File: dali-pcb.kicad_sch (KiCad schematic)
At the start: 2 parts

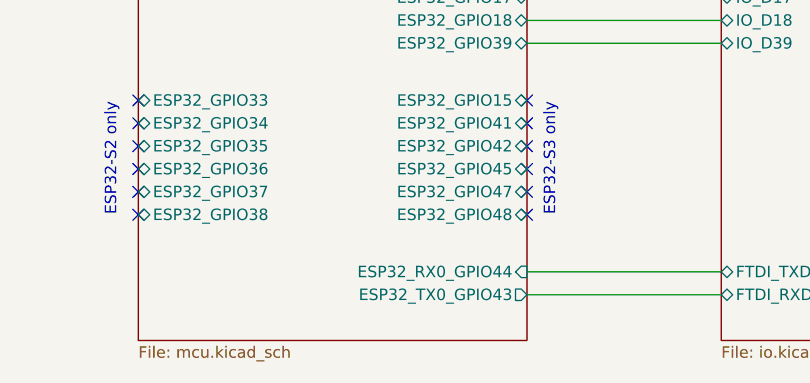
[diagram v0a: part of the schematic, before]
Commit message: Rename UART pins to use Espressif convention
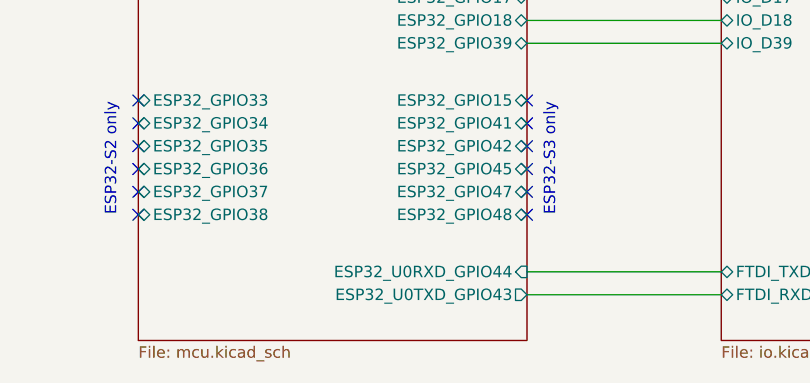
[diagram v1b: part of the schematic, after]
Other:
- sheet Microcontroller ports: added ESP32_U0RXD_GPIO44, ESP32_U0TXD_GPIO43; removed ESP32_RX0_GPIO44, ESP32_TX0_GPIO43
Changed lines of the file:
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@@
 			)
 		)
-		(pin "ESP32_RX0_GPIO44" input
+		(pin "ESP32_U0RXD_GPIO44" input
 			(at 144.78 82.55 0)
 			(effects
@@
 			)
 		)
-		(pin "ESP32_TX0_GPIO43" output
+		(pin "ESP32_U0TXD_GPIO43" output
 			(at 144.78 85.09 0)
 			(effects

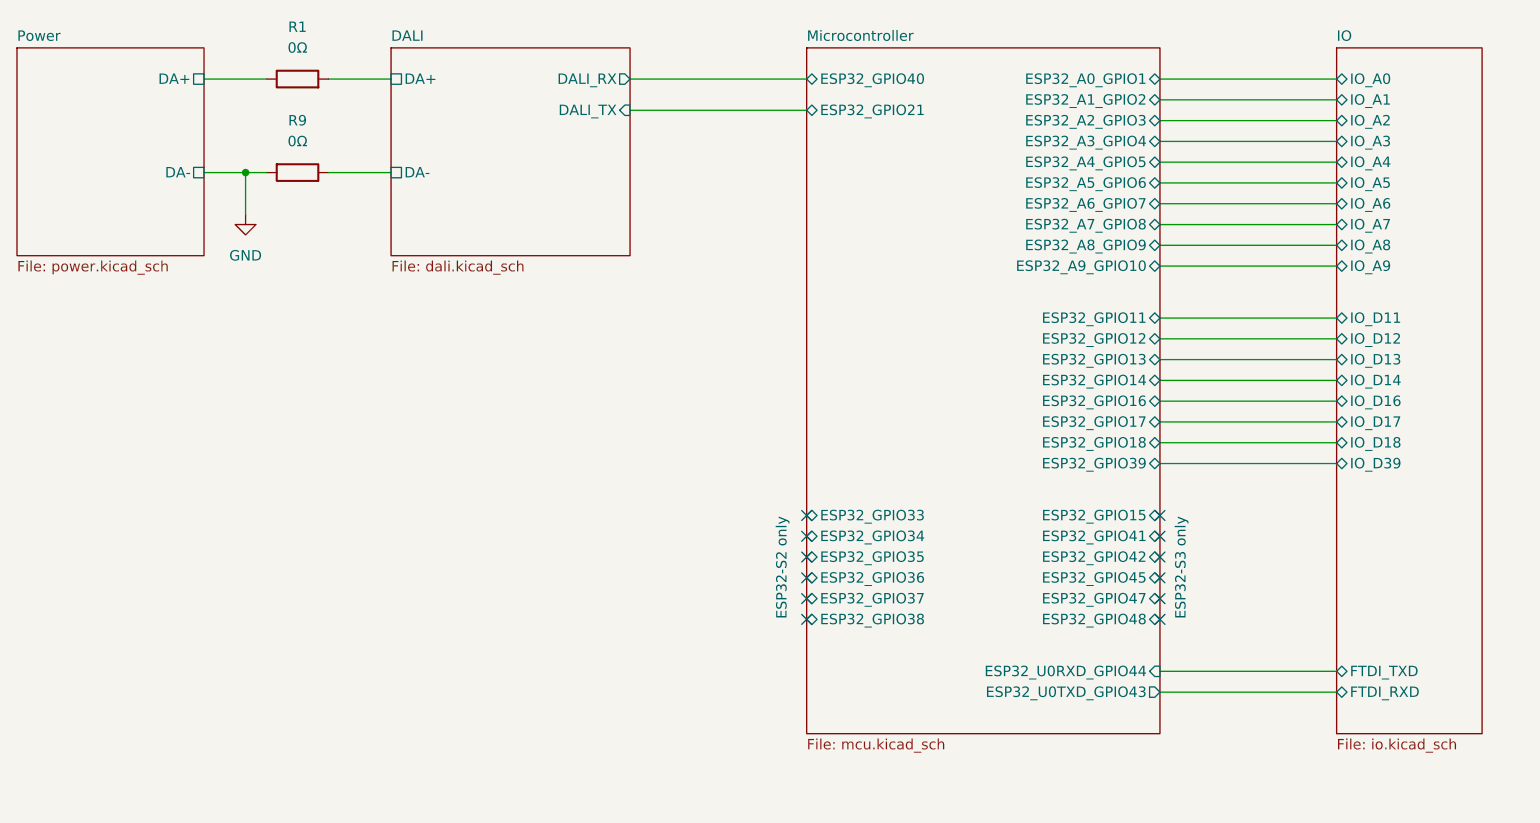
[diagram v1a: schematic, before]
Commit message: Add an FTDI connector for the DALI bus
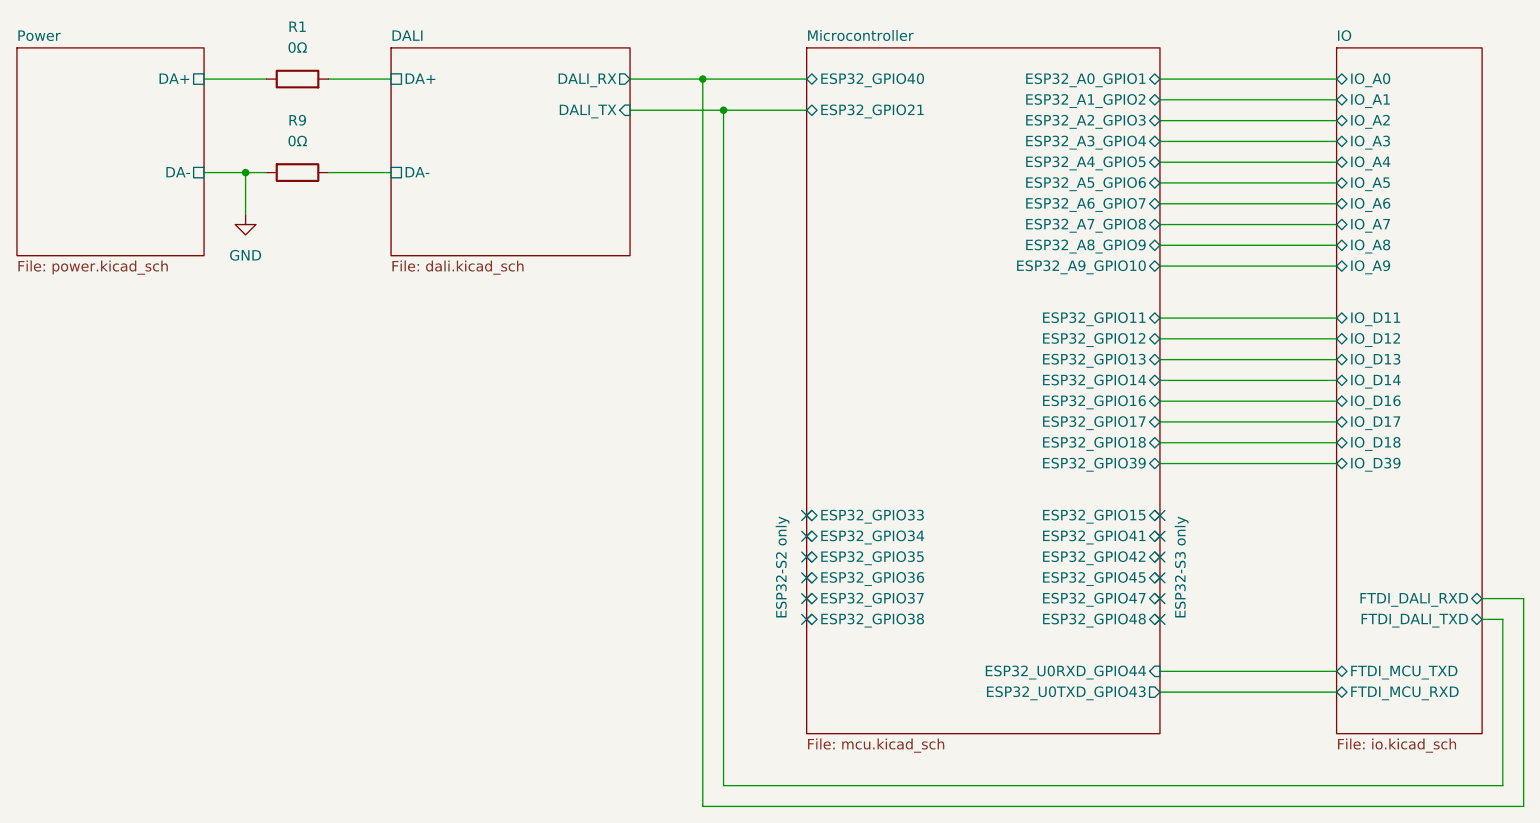
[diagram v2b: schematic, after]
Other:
- sheet IO ports: added FTDI_DALI_RXD, FTDI_DALI_TXD, FTDI_MCU_RXD, FTDI_MCU_TXD; removed FTDI_RXD, FTDI_TXD
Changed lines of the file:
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@@
 	(generator "eeschema")
 	(generator_version "9.0")
-	(paper "User" 190 100)
+	(paper "User" 195 105)
 	(text "ESP32-S2 only"
 		(exclude_from_sim no)
@@
 		(color 0 0 0 0)
 	)
+	(junction
+		(at 88.9 10.16)
+		(diameter 0)
+		(color 0 0 0 0)
+	)
+	(junction
+		(at 91.44 13.97)
+		(diameter 0)
+		(color 0 0 0 0)
+	)
 	(no_connect
 		(at 101.6 66.04)
@@
 	(wire
 		(pts
+			(xy 186.69 96.52) (xy 91.44 96.52)
+		)
+		(stroke
+			(width 0)
+			(type default)
+		)
+	)
+	(wire
+		(pts
 			(xy 144.78 54.61) (xy 166.37 54.61)
 		)
@@
 	(wire
 		(pts
+			(xy 189.23 73.66) (xy 189.23 99.06)
+		)
+		(stroke
+			(width 0)
+			(type default)
+		)
+	)
+	(wire
+		(pts
 			(xy 144.78 57.15) (xy 166.37 57.15)
 		)
@@
 	(wire
 		(pts
+			(xy 189.23 99.06) (xy 88.9 99.06)
+		)
+		(stroke
+			(width 0)
+			(type default)
+		)
+	)
+	(wire
+		(pts
 			(xy 144.78 12.7) (xy 166.37 12.7)
 		)
@@
 	(wire
 		(pts
+			(xy 91.44 13.97) (xy 101.6 13.97)
+		)
+		(stroke
+			(width 0)
+			(type default)
+		)
+	)
+	(wire
+		(pts
 			(xy 144.78 41.91) (xy 166.37 41.91)
 		)
@@
 	(wire
 		(pts
-			(xy 80.01 13.97) (xy 101.6 13.97)
+			(xy 80.01 13.97) (xy 91.44 13.97)
+		)
+		(stroke
+			(width 0)
+			(type default)
+		)
+	)
+	(wire
+		(pts
+			(xy 91.44 13.97) (xy 91.44 96.52)
 		)
 		(stroke
@@
 	(wire
 		(pts
-			(xy 80.01 10.16) (xy 101.6 10.16)
+			(xy 80.01 10.16) (xy 88.9 10.16)
 		)
 		(stroke
@@
 	(wire
 		(pts
+			(xy 184.15 76.2) (xy 186.69 76.2)
+		)
+		(stroke
+			(width 0)
+			(type default)
+		)
+	)
+	(wire
+		(pts
 			(xy 144.78 33.02) (xy 166.37 33.02)
 		)
@@
 	(wire
 		(pts
+			(xy 88.9 10.16) (xy 101.6 10.16)
+		)
+		(stroke
+			(width 0)
+			(type default)
+		)
+	)
+	(wire
+		(pts
 			(xy 144.78 82.55) (xy 166.37 82.55)
 		)
@@
 	(wire
 		(pts
+			(xy 88.9 10.16) (xy 88.9 99.06)
+		)
+		(stroke
+			(width 0)
+			(type default)
+		)
+	)
+	(wire
+		(pts
 			(xy 27.94 10.16) (xy 35.56 10.16)
 		)
@@
 	(wire
 		(pts
+			(xy 186.69 76.2) (xy 186.69 96.52)
+		)
+		(stroke
+			(width 0)
+			(type default)
+		)
+	)
+	(wire
+		(pts
 			(xy 33.02 21.59) (xy 35.56 21.59)
+		)
+		(stroke
+			(width 0)
+			(type default)
+		)
+	)
+	(wire
+		(pts
+			(xy 184.15 73.66) (xy 189.23 73.66)
 		)
 		(stroke
@@
 			)
 		)
-		(pin "FTDI_RXD" bidirectional
-			(at 166.37 85.09 180)
-			(effects
-				(font
-					(size 1.27 1.27)
-				)
-				(justify left)
-			)
-		)
-		(pin "FTDI_TXD" bidirectional
-			(at 166.37 82.55 180)
-			(effects
-				(font
-					(size 1.27 1.27)
-				)
-				(justify left)
-			)
-		)
 		(pin "IO_A0" bidirectional
 			(at 166.37 10.16 180)
@@
 			(effects
 				(font
+					(size 1.27 1.27)
+				)
+				(justify left)
+			)
+		)
+		(pin "FTDI_DALI_RXD" bidirectional
+			(at 184.15 73.66 0)
+			(effects
+				(font
+					(size 1.27 1.27)
+				)
+				(justify right)
+			)
+		)
+		(pin "FTDI_DALI_TXD" bidirectional
+			(at 184.15 76.2 0)
+			(effects
+				(font
+					(size 1.27 1.27)
+				)
+				(justify right)
+			)
+		)
+		(pin "FTDI_MCU_RXD" bidirectional
+			(at 166.37 85.09 180)
+			(effects
+				(font
+					(size 1.27 1.27)
+				)
+				(justify left)
+			)
+		)
+		(pin "FTDI_MCU_TXD" bidirectional
+			(at 166.37 82.55 180)
+			(effects
+				(font

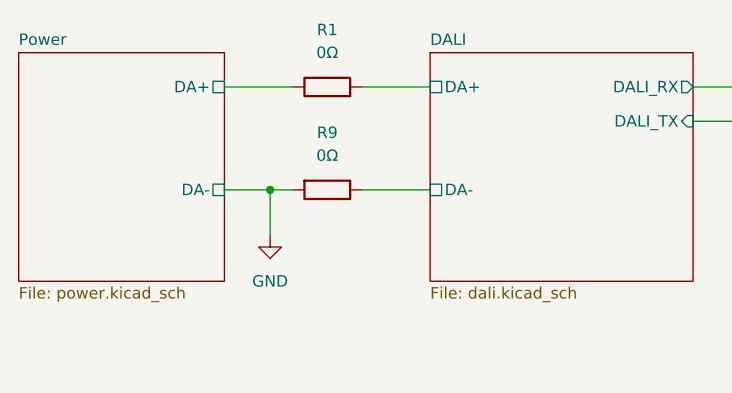
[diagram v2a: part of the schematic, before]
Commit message: Assign footprints to resistors and use solder jumpers
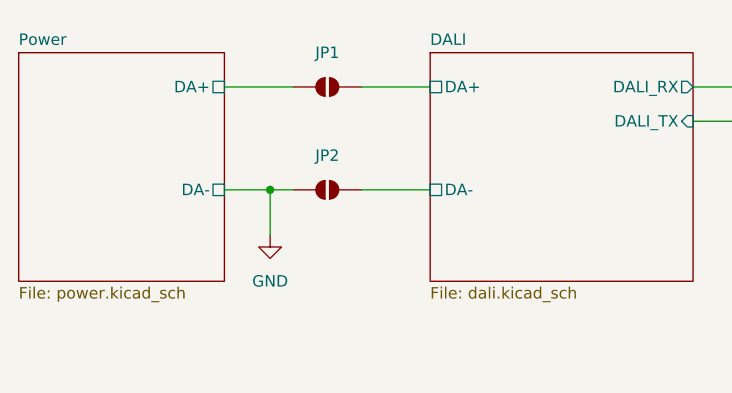
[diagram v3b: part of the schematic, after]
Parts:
- JP1: renamed from R1; value 0Ω -> SolderJumper_2_Open; footprint (none) -> Jumper:SolderJumper-2_P1.3mm_Open_RoundedPad1.0x1.5mm; symbol Device:R -> Jumper:SolderJumper_2_Open; now left out of the parts list
- JP2: renamed from R9; value 0Ω -> SolderJumper_2_Open; footprint (none) -> Jumper:SolderJumper-2_P1.3mm_Open_RoundedPad1.0x1.5mm; symbol Device:R -> Jumper:SolderJumper_2_Open; now left out of the parts list
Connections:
- net DALI/DA+: now also JP1.1 (A); no longer JP1.2
- net DALI/DA-: now also JP2.2 (B); no longer JP2.1
- net GND: now also JP2.1 (A); no longer JP2.2
- net Power/DA+: now also JP1.2 (B); no longer JP1.1
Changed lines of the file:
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@@
 	)
 	(symbol
-		(lib_id "Device:R")
-		(at 39.37 21.59 270)
+		(lib_id "Jumper:SolderJumper_2_Open")
+		(at 39.37 21.59 0)
 		(unit 1)
 		(exclude_from_sim no)
-		(in_bom yes)
+		(in_bom no)
 		(on_board yes)
 		(dnp no)
 		(fields_autoplaced yes)
-		(property "Reference" "R9"
-			(at 39.37 15.24 90)
+		(property "Reference" "JP2"
+			(at 39.37 17.78 0)
 			(effects
 				(font
@@
 			)
 		)
-		(property "Value" "0Ω"
-			(at 39.37 17.78 90)
+		(property "Value" "SolderJumper_2_Open"
+			(at 39.37 17.78 0)
 			(effects
 				(font
 					(size 1.27 1.27)
 				)
+				(hide yes)
 			)
 		)
-		(property "Footprint" ""
-			(at 39.37 19.812 90)
+		(property "Footprint" "Jumper:SolderJumper-2_P1.3mm_Open_RoundedPad1.0x1.5mm"
+			(at 39.37 21.59 0)
 			(effects
 				(font
@@
 			)
 		)
-		(property "Description" "Resistor"
+		(property "Description" "Solder Jumper, 2-pole, open"
 			(at 39.37 21.59 0)
 			(effects
@@
 			(project "dali-pcb"
 				(path "/aa7f7e07-1f39-4222-a272-c9975d033b6d"
-					(reference "R9")
+					(reference "JP2")
 					(unit 1)
 				)
@@
 	)
 	(symbol
-		(lib_id "Device:R")
-		(at 39.37 10.16 90)
+		(lib_id "Jumper:SolderJumper_2_Open")
+		(at 39.37 10.16 180)
 		(unit 1)
 		(exclude_from_sim no)
-		(in_bom yes)
+		(in_bom no)
 		(on_board yes)
 		(dnp no)
 		(fields_autoplaced yes)
-		(property "Reference" "R1"
-			(at 39.37 3.81 90)
+		(property "Reference" "JP1"
+			(at 39.37 6.35 0)
 			(effects
 				(font
@@
 			)
 		)
-		(property "Value" "0Ω"
-			(at 39.37 6.35 90)
+		(property "Value" "SolderJumper_2_Open"
+			(at 39.37 6.35 0)
 			(effects
 				(font
 					(size 1.27 1.27)
 				)
+				(hide yes)
 			)
 		)
-		(property "Footprint" ""
-			(at 39.37 11.938 90)
+		(property "Footprint" "Jumper:SolderJumper-2_P1.3mm_Open_RoundedPad1.0x1.5mm"
+			(at 39.37 10.16 0)
 			(effects
 				(font
@@
 			)
 		)
-		(property "Description" "Resistor"
+		(property "Description" "Solder Jumper, 2-pole, open"
 			(at 39.37 10.16 0)
 			(effects
@@
 			(project "dali-pcb"
 				(path "/aa7f7e07-1f39-4222-a272-c9975d033b6d"
-					(reference "R1")
+					(reference "JP1")
 					(unit 1)
 				)

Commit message: Place all components
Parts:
- added H1, H2, H3, H4: MountingHole_Pad, MountingHole:MountingHole_3.2mm_M3_Pad, symbol Mechanical:MountingHole_Pad
- JP1: value SolderJumper_2_Open -> POWER DA+
- JP2: value SolderJumper_2_Open -> POWER DA-
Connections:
- net GND: now also H1.1, H2.1, H3.1, H4.1

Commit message: FTDI TTL-232R-3V3 can't be used to directly interface with DALI
There's no 3.3V supply to use as a pull-up
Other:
- sheet IO ports: added UART_RX, UART_TX; removed FTDI_DALI_RXD, FTDI_DALI_TXD
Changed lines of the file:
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@@
 			)
 		)
-		(pin "FTDI_DALI_RXD" bidirectional
+		(pin "FTDI_MCU_RXD" input
+			(at 166.37 85.09 180)
+			(effects
+				(font
+					(size 1.27 1.27)
+				)
+				(justify left)
+			)
+		)
+		(pin "FTDI_MCU_TXD" output
+			(at 166.37 82.55 180)
+			(effects
+				(font
+					(size 1.27 1.27)
+				)
+				(justify left)
+			)
+		)
+		(pin "UART_RX" input
 			(at 184.15 73.66 0)
 			(effects
@@
 			)
 		)
-		(pin "FTDI_DALI_TXD" bidirectional
+		(pin "UART_TX" output
 			(at 184.15 76.2 0)
 			(effects
@@
 			)
 		)
-		(pin "FTDI_MCU_RXD" bidirectional
-			(at 166.37 85.09 180)
-			(effects
-				(font
-					(size 1.27 1.27)
-				)
-				(justify left)
-			)
-		)
-		(pin "FTDI_MCU_TXD" bidirectional
-			(at 166.37 82.55 180)
-			(effects
-				(font
-					(size 1.27 1.27)
-				)
-				(justify left)
-			)
-		)

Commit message: Add LOLIN S3 mini support
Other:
- note added: "LOLIN-S2/S3-MINI only"
- note removed: "ESP32-S2 only"
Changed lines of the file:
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@@
 	(generator_version "9.0")
 	(paper "User" 195 105)
-	(text "ESP32-S2 only"
+	(text "LOLIN-S2/S3-MINI only"
 		(exclude_from_sim no)
 		(at 98.552 70.104 90)
